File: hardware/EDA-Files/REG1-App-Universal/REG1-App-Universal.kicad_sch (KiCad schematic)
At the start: 13 parts, among them J1 REG1_App_Connector, J10 Conn_01x06, J11 Conn_01x06, J2 Conn_01x10, J20 Conn_01x06, J21 Conn_01x06, J30 Conn_01x22, J31 Conn_01x22, J32 Conn_01x22, J33 Conn_01x22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

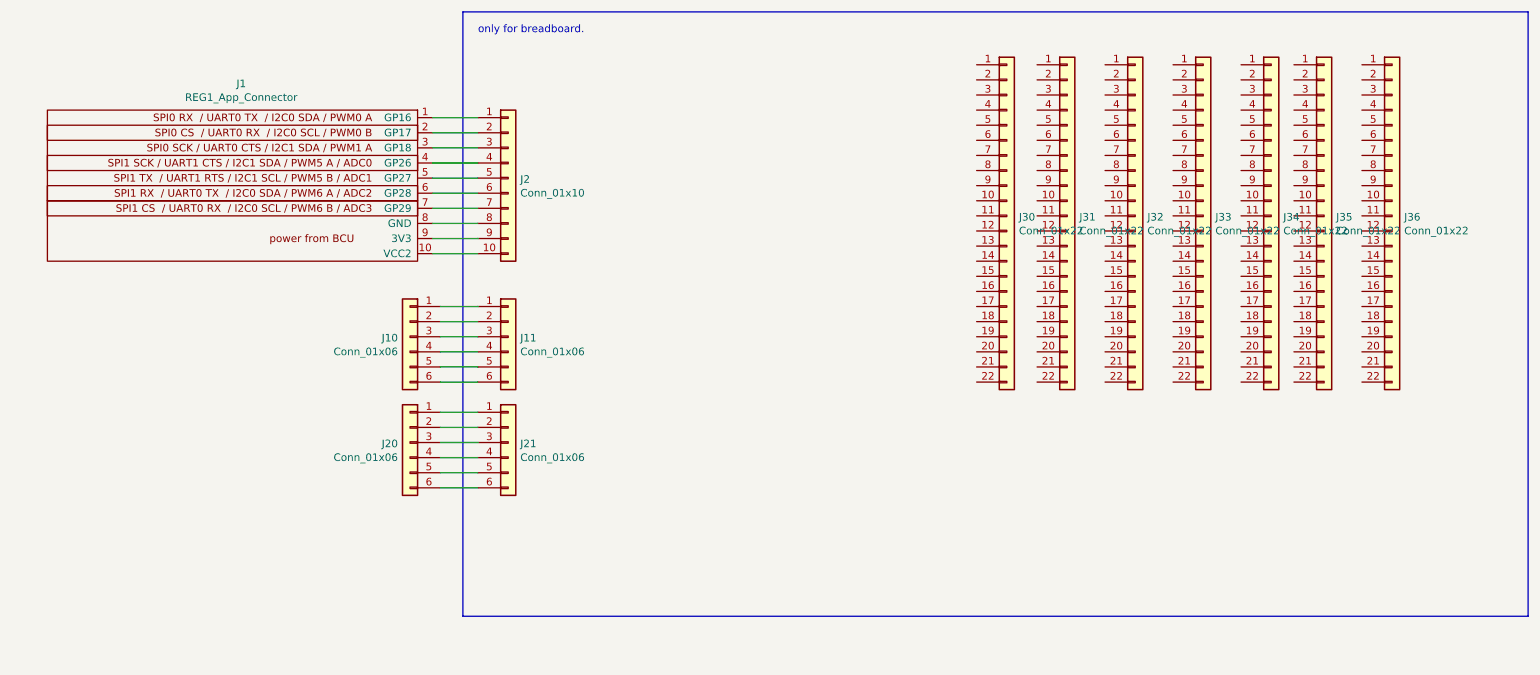
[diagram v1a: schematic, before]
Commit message: REG1-App-Universal - editorial rework V01.10
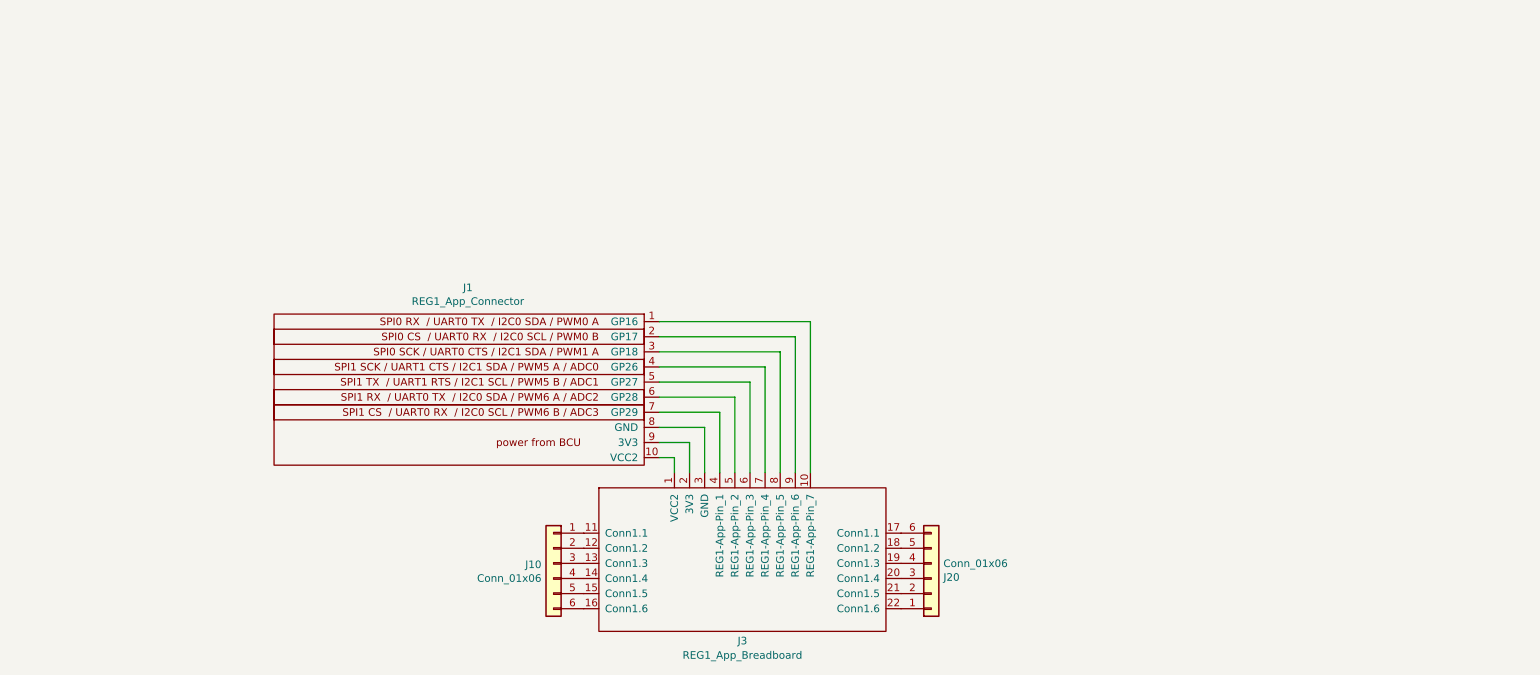
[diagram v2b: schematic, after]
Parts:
- removed J11, J21: Conn_01x06, Connector_PinHeader_2.54mm:PinHeader_1x06_P2.54mm_Vertical, symbol Connector_Generic:Conn_01x06
- removed J2: Conn_01x10, Connector_PinHeader_2.54mm:PinHeader_1x10_P2.54mm_Vertical, symbol Connector_Generic:Conn_01x10
- removed J30, J31, J32, J33, J34, J35, J36: Conn_01x22, Connector_PinHeader_2.54mm:PinHeader_1x22_P2.54mm_Vertical, symbol Connector_Generic:Conn_01x22
- added J3: REG1_App_Breadboard, OpenKNX:REG1_App_Breadboard, symbol OpenKNX:REG_App_Breadboard
- J1: LCSC (none) -> C706873
- J10, J20: LCSC (none) -> C441175
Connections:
- net at J10.1 (Pin_1): now also J3.11 (Conn1.1)
- net at J10.2 (Pin_2): now also J3.12 (Conn1.2)
- net at J10.3 (Pin_3): now also J3.13 (Conn1.3)
- net at J10.4 (Pin_4): now also J3.14 (Conn1.4)
- net at J10.5 (Pin_5): now also J3.15 (Conn1.5)
- net at J10.6 (Pin_6): now also J3.16 (Conn1.6)
- net at J20.1 (Pin_1): now also J3.22 (Conn1.6)
- net at J20.2 (Pin_2): now also J3.21 (Conn1.5)
- net at J20.3 (Pin_3): now also J3.20 (Conn1.4)
- net at J20.4 (Pin_4): now also J3.19 (Conn1.3)
- net at J20.5 (Pin_5): now also J3.18 (Conn1.2)
- net at J20.6 (Pin_6): now also J3.17 (Conn1.1)
- net at J1.1 (GP16): now also J3.10 (REG1-App-Pin_7)
- net at J1.10 (VCC2): now also J3.1 (VCC2)
- net at J1.2 (GP17): now also J3.9 (REG1-App-Pin_6)
- net at J1.3 (GP18): now also J3.8 (REG1-App-Pin_5)
- net at J1.4 (GP26): now also J3.7 (REG1-App-Pin_4)
- net at J1.5 (GP27): now also J3.6 (REG1-App-Pin_3)
- net at J1.6 (GP28): now also J3.5 (REG1-App-Pin_2)
- net at J1.7 (GP29): now also J3.4 (REG1-App-Pin_1)
- net at J1.8 (GND): now also J3.3 (GND)
- net at J1.9 (3V3): now also J3.2 (3V3)
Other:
- note removed: "only for breadboard."
- moved on the sheet: J1, J10, J20
